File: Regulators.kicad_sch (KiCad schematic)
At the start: 37 parts, among them J15 24V Peripheral, J5 24V Logic, U2 TPS5430DDAR, U3 TPS5430DDAR, U4 TPS5430DDAR

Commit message: Fixes to screw terminal footprints, updated BOM and included in project folder
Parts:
- J15, J5: footprint OSTVTerminalBlocks:Conn01x02 -> EBWA_02_A:ADAMTECH_EBWA-02-A
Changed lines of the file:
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@@
 			)
 		)
-		(property "Footprint" "OSTVTerminalBlocks:Conn01x02"
+		(property "Footprint" "EBWA_02_A:ADAMTECH_EBWA-02-A"
 			(at 24.13 40.64 0)
 			(effects
@@
 			)
 		)
-		(property "Footprint" "OSTVTerminalBlocks:Conn01x02"
+		(property "Footprint" "EBWA_02_A:ADAMTECH_EBWA-02-A"
 			(at 34.29 104.14 0)
 			(effects

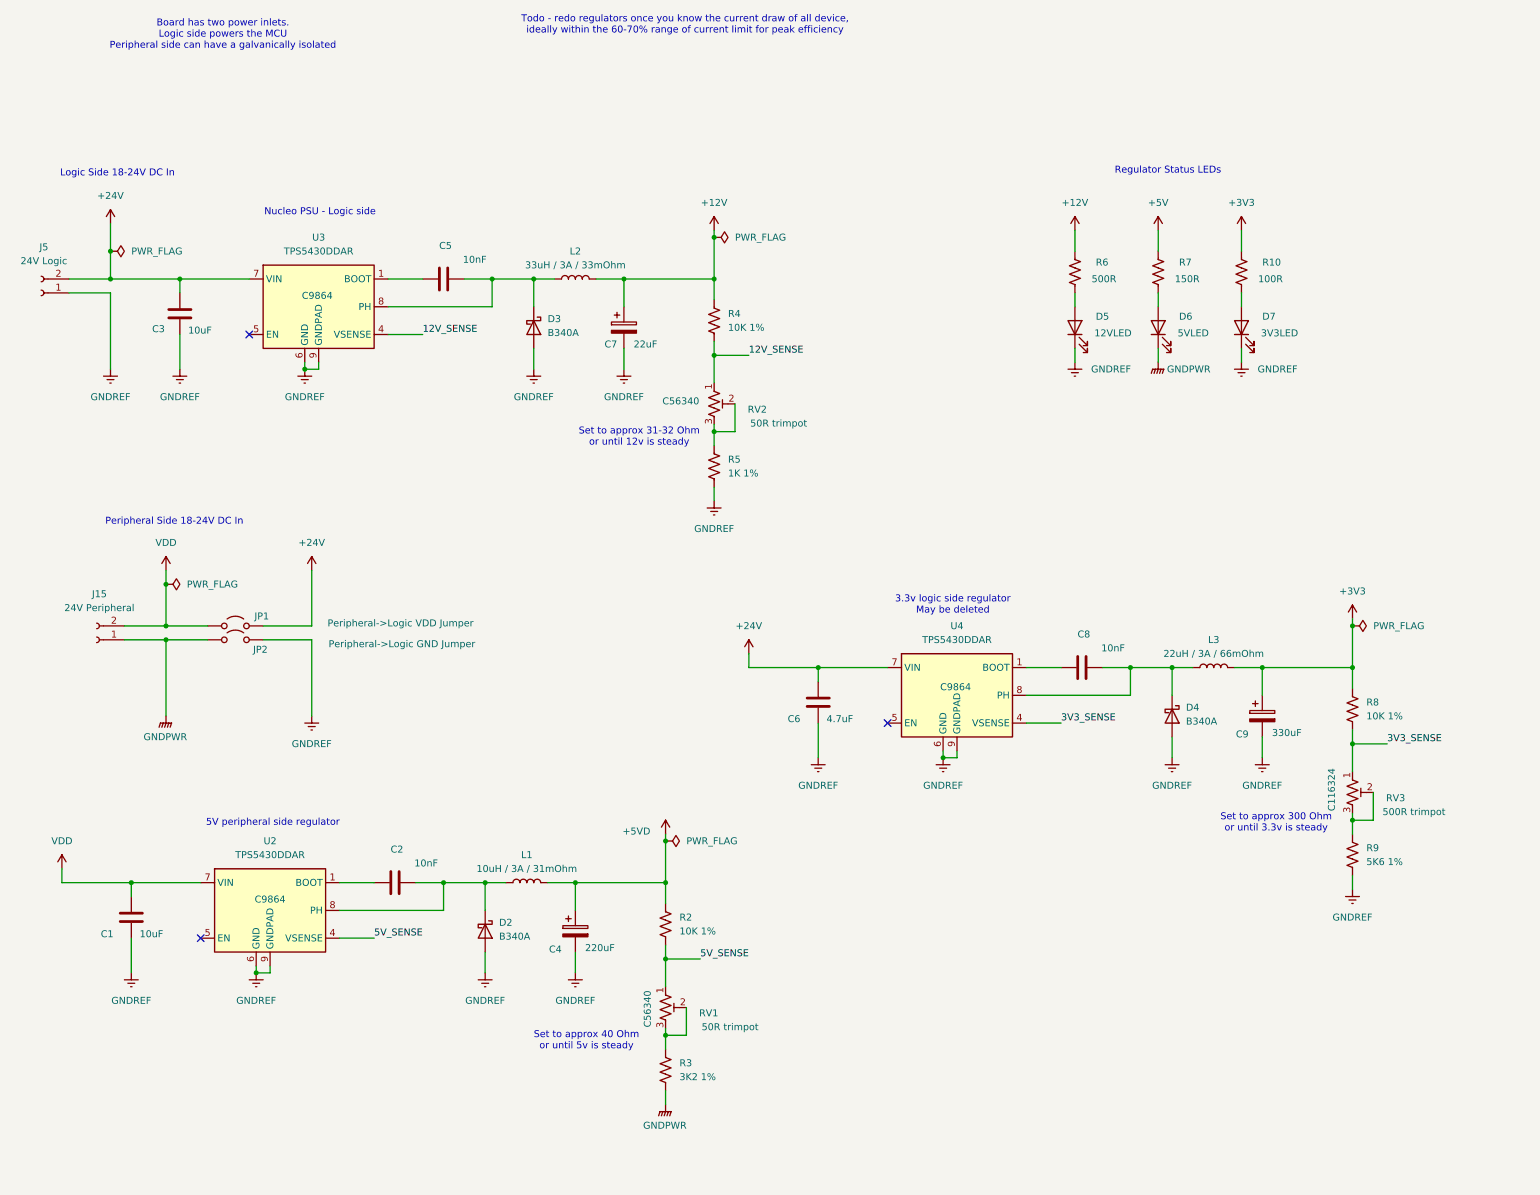
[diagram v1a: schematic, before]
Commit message: updates to read me, marked V1 parts inactive and made start on board layout for initial test board. fixes to BOM to suit
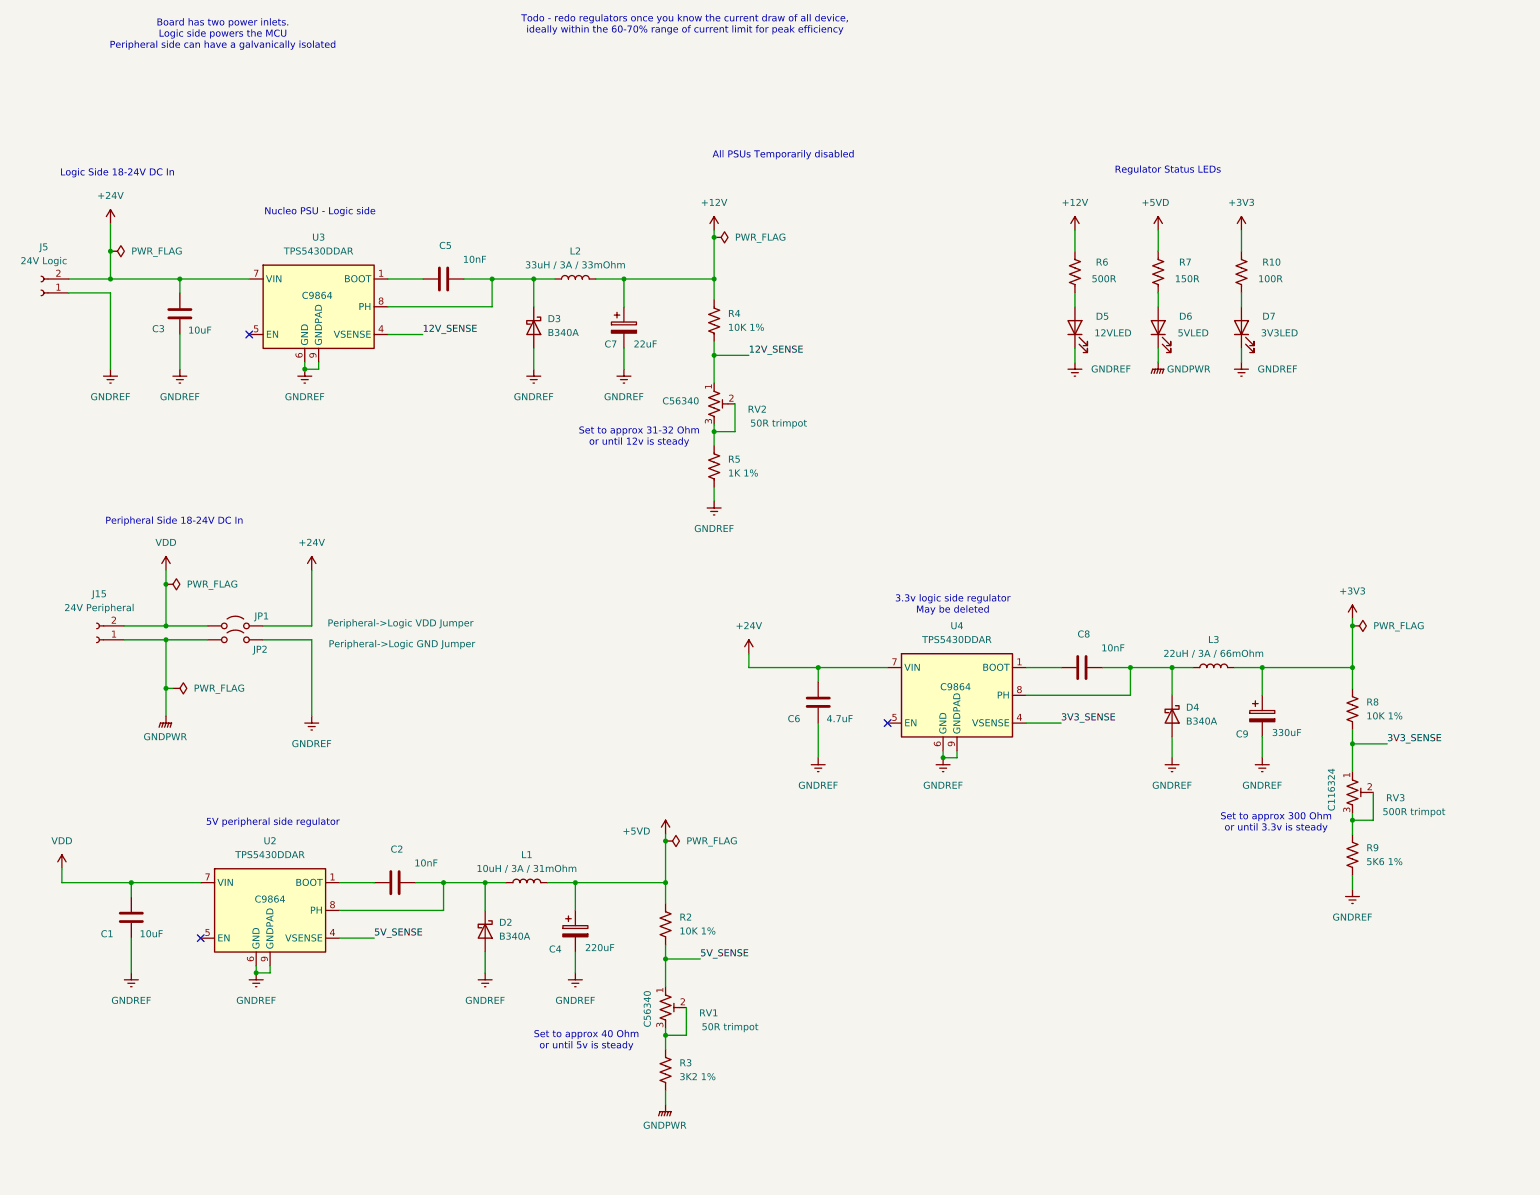
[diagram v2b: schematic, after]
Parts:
- JP1, JP2: footprint (none) -> Jumper:SolderJumper-2_P1.3mm_Open_RoundedPad1.0x1.5mm
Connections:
- net +5V is gone; now on net +5VD: R7.1
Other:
- note added: "All PSUs Temporarily disabled"

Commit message: New optocoupler part choice, removed digikey BOM as have started inputting them into symbol fields. Re-enabled all disabled parts for now and will re-design power supplies soon.
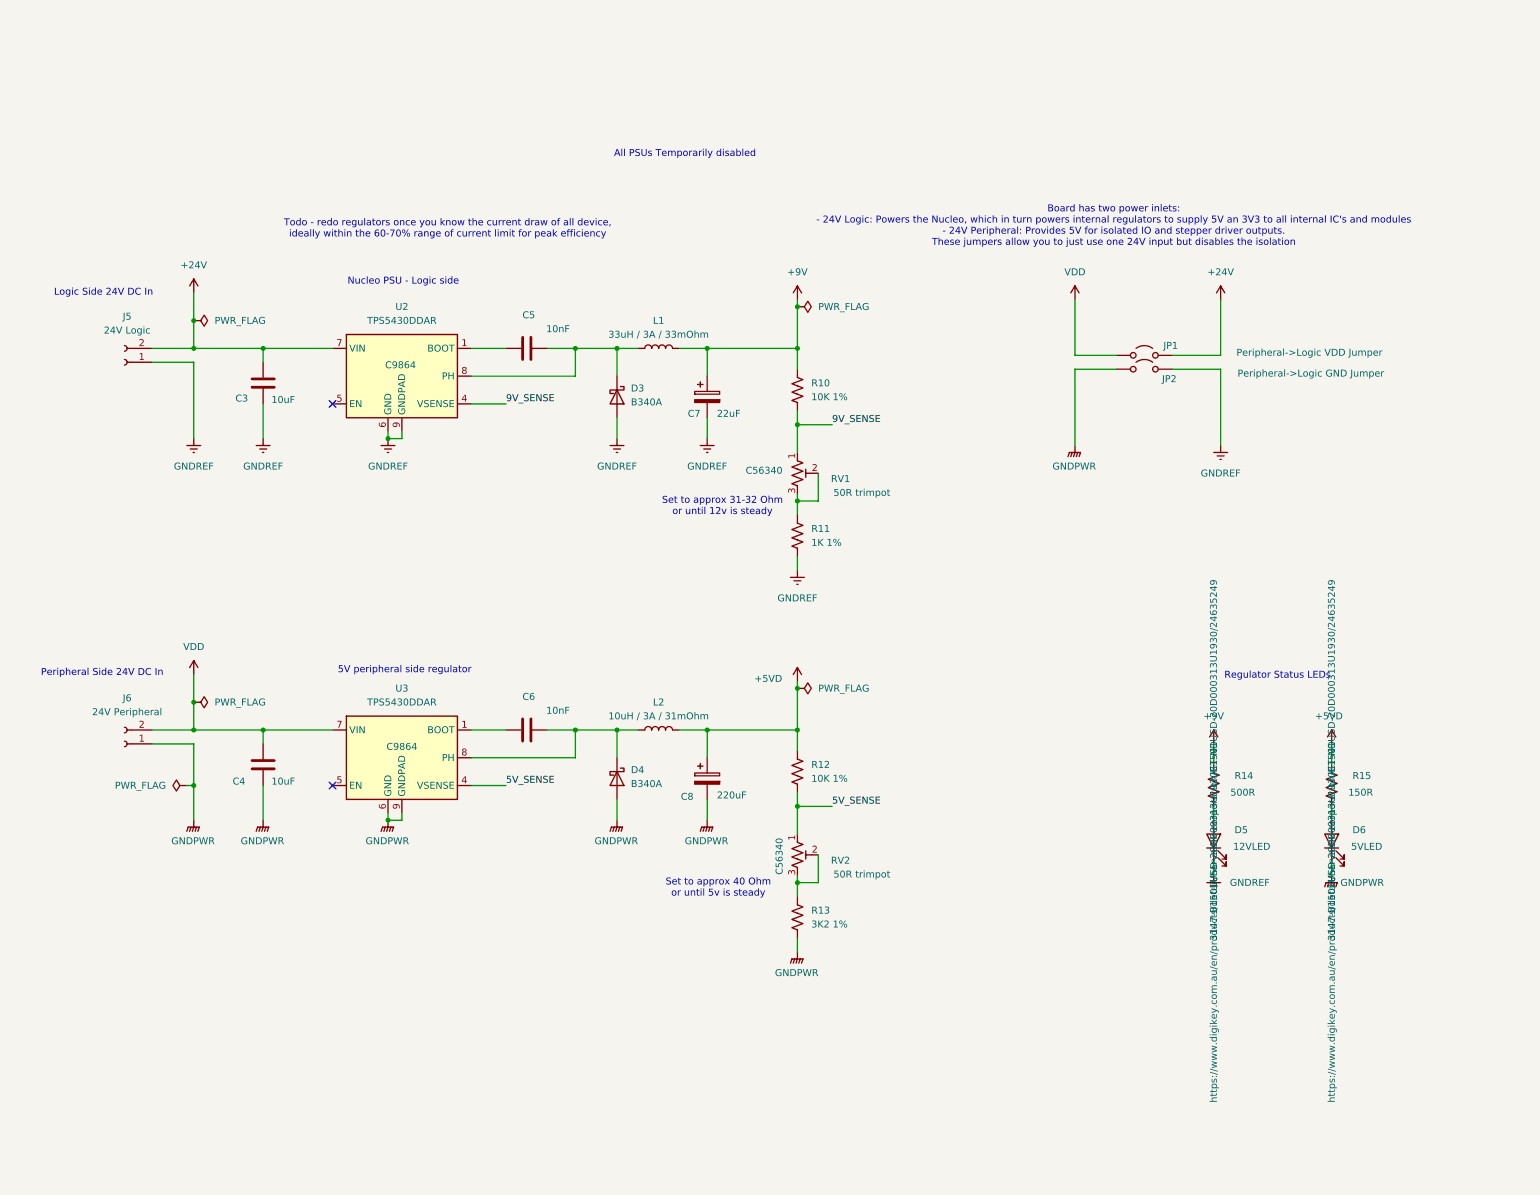
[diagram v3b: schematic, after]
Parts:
- removed C6: 4.7uF, symbol Device:C
- removed C8: 10nF, Capacitor_SMD:C_1206_3216Metric_Pad1.33x1.80mm_HandSolder, symbol Device:C
- removed C9: 330uF, symbol Device:C_Polarized
- removed D4: B340A, Diode_SMD:D_1206_3216Metric_Pad1.42x1.75mm_HandSolder, symbol Device:D_Schottky
- removed D7: 3V3LED, Diode_SMD:D_1206_3216Metric_Pad1.42x1.75mm_HandSolder, symbol Device:LED
- removed L3: 22uH / 3A / 66mOhm, symbol Device:L
- removed R10: 100R, Resistor_SMD:R_1206_3216Metric_Pad1.30x1.75mm_HandSolder, symbol Device:R_US
- removed R8: 10K 1%, Resistor_SMD:R_1206_3216Metric_Pad1.30x1.75mm_HandSolder, symbol Device:R_US
- removed R9: 5K6 1%, Resistor_SMD:R_1206_3216Metric_Pad1.30x1.75mm_HandSolder, symbol Device:R_US
- removed RV3: 500R trimpot, Potentiometer_SMD:Potentiometer_Bourns_3224W_Vertical, symbol Device:R_Potentiometer_Trim_US
- removed U4: TPS5430DDAR, Package_SO:TI_SO-PowerPAD-8_ThermalVias, symbol Regulator_Switching:TPS5430DDA
- D5, D6: Digikey Part Number (none) -> 3147-B1501USD-20D000313U1930CT-ND; Digikey URL (none) -> https://www.digikey.com.au/en/products/detail/harvatek-corp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
- J5: now in the parts list
- J6: renamed from J15; now in the parts list
- renumbered C1 to C4, C2 to C6, C4 to C8, D2 to D4, L2 to L1, L1 to L2, R4 to R10, R5 to R11, R2 to R12, R3 to R13, R6 to R14, R7 to R15, RV2 to RV1, RV1 to RV2, U3 to U2, U2 to U3
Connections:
- net GNDPWR: now also C4.2, C8.2, D4.2 (A), U3.6 (GND), U3.9 (GNDPAD)
- net GNDREF: no longer C4.2, C8.2, D4.2 (A), U3.6 (GND), U3.9 (GNDPAD)
- net +12V renamed +9V
- net 12V_SENSE renamed 9V_SENSE
- no-connect marks 3 -> 2
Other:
- note added: "Board has two power inlets: - 24V Logic: Powers the Nucleo, which in turn powers internal regulators to supply 5V an 3V3 to all internal IC's and modules - 24V Peripheral: Provides 5V for isolated IO and stepper driver outputs. These jumpers allow you to just use one 24V input but disables the isolation"
- note added: "Logic Side 24V DC In"
- note added: "Peripheral Side 24V DC In"
- note removed: "3.3v logic side regulator May be deleted"
- note removed: "Board has two power inlets. Logic side powers the MCU Peripheral side can have a galvanically isolated"
- note removed: "Logic Side 18-24V DC In"
- note removed: "Peripheral Side 18-24V DC In"
- note removed: "Set to approx 300 Ohm or until 3.3v is steady"
- moved on the sheet: C3, C4, C5, C6, C7, C8, D3, D4, D5, D6, J5, J6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

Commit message: fix to annoying additional symbol fields displaying when we didn't want them to.
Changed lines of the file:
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@@
 					(size 1.27 1.27)
 				)
+				(hide yes)
 			)
 		)
@@
 					(size 1.27 1.27)
 				)
+				(hide yes)
 			)
 		)
@@
 					(size 1.27 1.27)
 				)
+				(hide yes)
 			)
 		)
@@
 					(size 1.27 1.27)
 				)
+				(hide yes)
 			)
 		)
@@
 					(size 1.27 1.27)
 				)
+				(hide yes)
 			)
 		)
@@
 					(size 1.27 1.27)
 				)
+				(hide yes)
 			)
 		)
@@
 					(size 1.27 1.27)
 				)
+				(hide yes)
 			)
 		)
@@
 					(size 1.27 1.27)
 				)
+				(hide yes)
 			)
 		)
@@
 					(size 1.27 1.27)
 				)
+				(hide yes)
 			)
 		)
@@
 					(size 1.27 1.27)
 				)
+				(hide yes)
 			)
 		)
@@
 					(size 1.27 1.27)
 				)
+				(hide yes)
 			)
 		)
@@
 					(size 1.27 1.27)
 				)
+				(hide yes)
 			)
 		)
@@
 					(size 1.27 1.27)
 				)
+				(hide yes)
 			)
 		)
@@
 					(size 1.27 1.27)
 				)
+				(hide yes)
 			)
 		)
@@
 					(size 1.27 1.27)
 				)
+				(hide yes)
 			)
 		)
@@
 					(size 1.27 1.27)
 				)
+				(hide yes)
 			)
 		)
@@
 					(size 1.27 1.27)
 				)
+				(hide yes)
 			)
 		)
@@
 					(size 1.27 1.27)
 				)
+				(hide yes)
 			)
 		)
@@
 					(size 1.27 1.27)
 				)
+				(hide yes)
 			)
 		)
@@
 					(size 1.27 1.27)
 				)
+				(hide yes)
 			)
 		)
@@
 					(size 1.27 1.27)
 				)
+				(hide yes)
 			)
 		)
@@
 					(size 1.27 1.27)
 				)
+				(hide yes)
 			)
 		)
@@
 					(size 1.27 1.27)
 				)
+				(hide yes)
 			)
 		)
@@
 					(size 1.27 1.27)
 				)
+				(hide yes)
 			)
 		)
@@
 					(size 1.27 1.27)
 				)
+				(hide yes)
 			)
 		)
@@
 					(size 1.27 1.27)
 				)
+				(hide yes)
 			)
 		)
@@
 					(size 1.27 1.27)
 				)
+				(hide yes)
 			)
 		)
@@
 					(size 1.27 1.27)
 				)
+				(hide yes)
 			)
 		)
@@
 					(size 1.27 1.27)
 				)
+				(hide yes)
 			)
 		)
@@
 					(size 1.27 1.27)
 				)
+				(hide yes)
 			)
 		)
@@
 					(size 1.27 1.27)
 				)
+				(hide yes)
 			)
 		)
@@
 					(size 1.27 1.27)
 				)
+				(hide yes)
 			)
 		)
@@
 					(size 1.27 1.27)
 				)
+				(hide yes)
 			)
 		)
@@
 					(size 1.27 1.27)
 				)
+				(hide yes)
 			)
 		)
@@
 					(size 1.27 1.27)
 				)
+				(hide yes)
 			)
 		)
@@
 					(size 1.27 1.27)
 				)
+				(hide yes)
 			)
 		)
@@
 					(size 1.27 1.27)
 				)
+				(hide yes)
 			)
 		)
@@
 					(size 1.27 1.27)
 				)
+				(hide yes)
 			)
 		)
@@
 					(size 1.27 1.27)
 				)
+				(hide yes)
 			)
 		)
@@
 					(size 1.27 1.27)
 				)
+				(hide yes)
 			)
 		)
@@
 					(size 1.27 1.27)
 				)
+				(hide yes)
 			)
 		)
@@
 					(size 1.27 1.27)
 				)
+				(hide yes)
 			)
 		)
@@
 					(size 1.27 1.27)
 				)
+				(hide yes)
 			)
 		)
@@
 					(size 1.27 1.27)
 				)
+				(hide yes)
 			)
 		)
@@
 					(size 1.27 1.27)
 				)
+				(hide yes)
 			)
 		)
@@
 					(size 1.27 1.27)
 				)
+				(hide yes)
 			)
 		)
@@
 					(size 1.27 1.27)
 				)
+				(hide yes)
 			)
 		)
@@
 					(size 1.27 1.27)
 				)
+				(hide yes)
 			)
 		)
@@
 					(size 1.27 1.27)
 				)
+				(hide yes)
 			)
 		)
@@
 					(size 1.27 1.27)
 				)
+				(hide yes)
 			)
 		)
@@
 					(size 1.27 1.27)
 				)
+				(hide yes)
 			)
 		)
@@
 					(size 1.27 1.27)
 				)
+				(hide yes)
 			)
 		)
@@
 					(size 1.27 1.27)
 				)
+				(hide yes)
 			)
 		)
@@
 					(size 1.27 1.27)
 				)
+				(hide yes)
 			)
 		)
@@
 					(size 1.27 1.27)
 				)
+				(hide yes)
 			)
 		)
@@
 					(size 1.27 1.27)
 				)
+				(hide yes)
 			)
 		)
